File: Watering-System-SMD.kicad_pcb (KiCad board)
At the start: 2 copper layers, 76 x 30 mm, 20 parts, among them CON1 AVR-ISP-6, J1 Screw_Terminal_1x02, J2 CONN_01X04_MALE, J3 Screw_Terminal_1x04, J4 Screw_Terminal_1x02, Q1 MMBF170, Q2 2N7002, U1 MCP1703A-3302/MB, U2 ATTINY84-20SSU

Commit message: PCB routed
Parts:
- added M3: MountingHole_3.2mm_M3, Mounting_Holes:MountingHole_3.2mm_M3, F.Cu at (57.0, 95.0)
- added M3: MountingHole_3.2mm_M3, Mounting_Holes:MountingHole_3.2mm_M3, F.Cu at (125.0, 95.0)
- added U3: ESP-01, ESP8266:ESP-01, F.Cu at (98.8, 81.2)
- C3, D2, R1, R2: moved to B.Cu
- moved J2 24.1 mm to (68.7, 71.0), turned to 90 degrees
- moved C1 16.8 mm to (117.0, 90.5), turned to 90 degrees
- moved R5 15.5 mm to (107.5, 80.2), turned to 180 degrees
- moved R3 13.2 mm to (107.5, 82.5), turned to 180 degrees
- moved D1 11.8 mm to (121.2, 85.8), turned to 90 degrees
- moved Q2 11.6 mm to (56.8, 84.8), turned to 180 degrees
- moved U1 11.2 mm to (111.5, 90.5), turned to 0 degrees
- moved C2 10.2 mm to (106.5, 90.8), turned to 90 degrees
- moved C3 10.1 mm to (74.2, 89.5), turned to 90 degrees
- moved Q1 9.04 mm to (113.0, 81.2), turned to 90 degrees
- moved R4 7.77 mm to (61.9, 83.8)
- moved R6 7.65 mm to (61.9, 86.2)
- moved CON1 7.32 mm to (97.5, 88.2), turned to 270 degrees
- moved R1 4.74 mm to (56.2, 80.2)
- moved D2 4.07 mm to (112.5, 78.0)
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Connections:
- U2 pad 10: /RX -> /TX
- U2 pad 11: /TX -> /RX
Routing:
- net VCC: track 4.12 -> 136.3 mm, vias 0 -> 1
- net /SCL: track 0.00 -> 77.1 mm
- net /SDA: track 0.00 -> 72.4 mm
- net GND: track 0.00 -> 62.2 mm, vias 0 -> 2
- net /RX: track 0.00 -> 43.9 mm
- net /TX: track 0.00 -> 42.0 mm
- net /EV_ON: track 0.00 -> 33.6 mm, vias 0 -> 1
- net /SENSOR_ON: track 0.00 -> 19.9 mm
- net /RST: track 0.00 -> 19.4 mm, vias 0 -> 1
- net /EV_CONN: track 0.00 -> 13.6 mm
- net /SENSOR_CONN: track 0.00 -> 12.9 mm
- net Net-(Q1-Pad1): track 0.00 -> 4.11 mm
- net Net-(Q2-Pad1): track 0.00 -> 2.98 mm
- net Net-(C1-Pad1): track 15.0 -> 16.7 mm
- added copper zone on B.Cu, net GND
- added copper zone on F.Cu, net GND
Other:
- board text added: "9-12V/GND"
- board text added: "E.V."

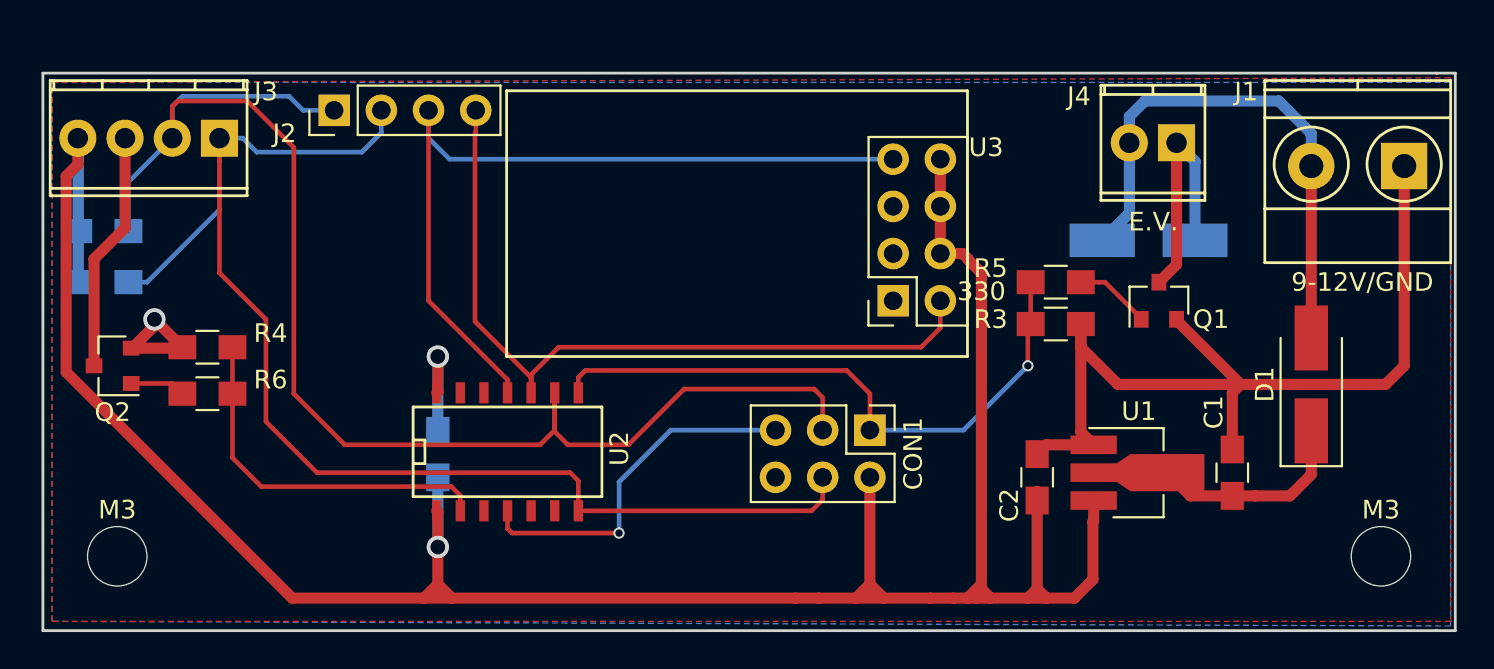
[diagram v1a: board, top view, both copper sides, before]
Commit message: SilkScreen changed
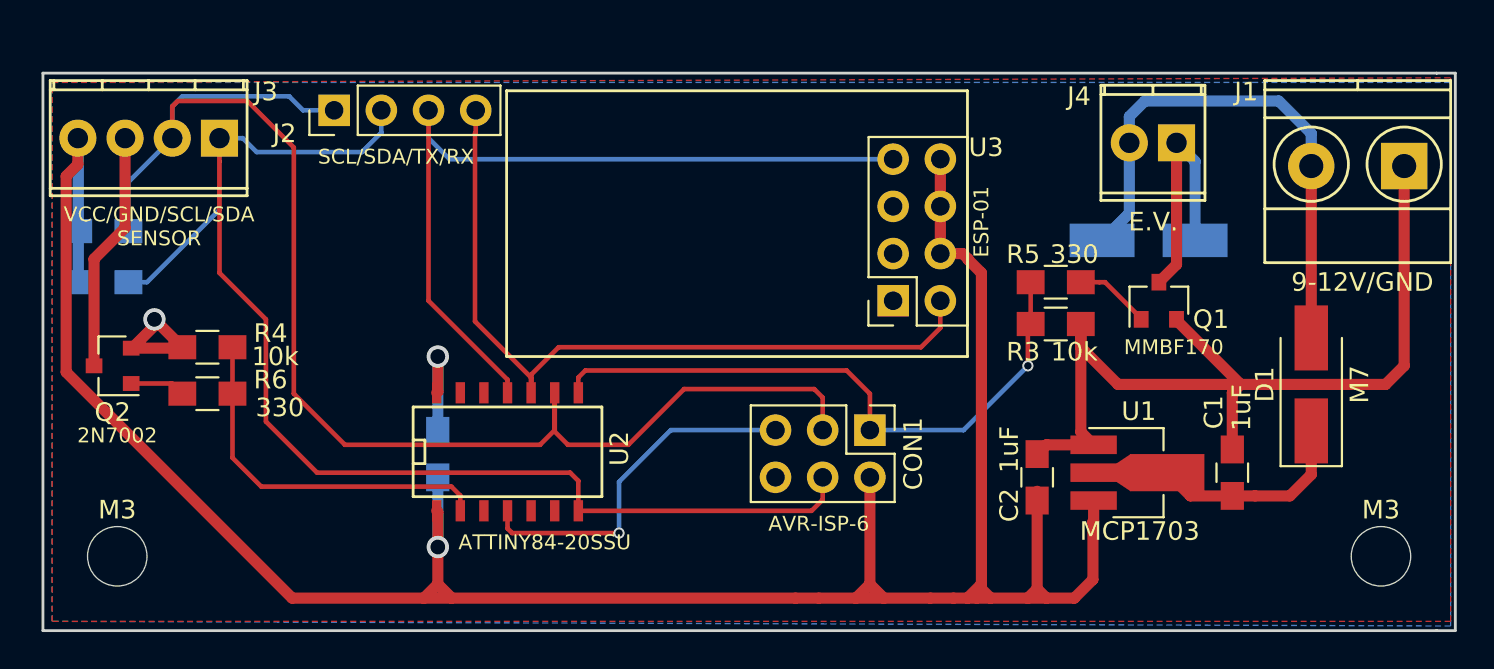
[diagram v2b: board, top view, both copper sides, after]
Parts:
- D1, D2: value D -> M7
- U1: value MCP1703A-3302/MB -> MCP1703
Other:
- board text added: "SCL/SDA/TX/RX"
- board text added: "VCC/GND/SCL/SDA SENSOR"
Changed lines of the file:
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@@
     (links 51)
     (no_connects 0)
-    (area 36.72143 63.678571 145.202382 108.7)
+    (area 52.924999 68.924999 129.075001 99.075001)
     (thickness 1.6)
-    (drawings 10)
+    (drawings 12)
     (tracks 189)
     (zones 0)
@@
   (page A4)
   (layers
-    (0 F.Cu signal)
-    (31 B.Cu signal)
+    (0 F.Cu signal hide)
+    (31 B.Cu signal hide)
     (32 B.Adhes user)
     (33 F.Adhes user)
@@
       (effects (font (size 1 1) (thickness 0.15)))
     )
-    (fp_text value ESP-01 (at 3.4925 5.08 90) (layer F.Fab)
-      (effects (font (size 1 1) (thickness 0.15)))
+    (fp_text value ESP-01 (at 4.25 4.75 90) (layer F.SilkS)
+      (effects (font (size 0.8 0.8) (thickness 0.15)))
     )
     (fp_line (start -3 -20.8) (end -3 4) (layer F.SilkS) (width 0.15))
@@
       (effects (font (size 1 1) (thickness 0.15)))
     )
-    (fp_text value 1uF (at 3.5 0.5 90) (layer F.Fab)
+    (fp_text value 1uF (at 3.5 0.5 90) (layer F.SilkS)
       (effects (font (size 1 1) (thickness 0.15)))
     )
@@
       (effects (font (size 1 1) (thickness 0.15)))
     )
-    (fp_text value 1uF (at 1.5 -1.5 90) (layer F.Fab)
+    (fp_text value 1uF (at 1.5 -1.5 90) (layer F.SilkS)
       (effects (font (size 1 1) (thickness 0.15)))
     )
@@
       (effects (font (size 1 1) (thickness 0.15)) (justify mirror))
     )
-    (fp_text value 0.1uF (at 0 -1.75 90) (layer B.Fab)
+    (fp_text value 0.1uF (at 0 -1.75 90) (layer B.SilkS)
       (effects (font (size 1 1) (thickness 0.15)) (justify mirror))
     )
@@
       (effects (font (size 1 1) (thickness 0.15)))
     )
-    (fp_text value AVR-ISP-6 (at 1.27 7.41 270) (layer F.Fab)
-      (effects (font (size 1 1) (thickness 0.15)))
+    (fp_text value AVR-ISP-6 (at 5.04 2.75 360) (layer F.SilkS)
+      (effects (font (size 0.8 0.8) (thickness 0.15)))
     )
     (fp_line (start -1.27 -1.27) (end -1.27 6.35) (layer F.Fab) (width 0.1))
@@
       (effects (font (size 1 1) (thickness 0.15)))
     )
-    (fp_text value MMBF170 (at -2.5 0.8 360) (layer F.Fab)
-      (effects (font (size 1 1) (thickness 0.15)))
+    (fp_text value MMBF170 (at -2.5 0.8 180) (layer F.SilkS)
+      (effects (font (size 0.8 0.8) (thickness 0.15)))
     )
     (fp_text user %R (at 0 0 90) (layer F.Fab)
@@
       (effects (font (size 1 1) (thickness 0.15)))
     )
-    (fp_text value 2N7002 (at 0 2.5 180) (layer F.Fab)
-      (effects (font (size 1 1) (thickness 0.15)))
+    (fp_text value 2N7002 (at -0.25 -3.75 180) (layer F.SilkS)
+      (effects (font (size 0.8 0.8) (thickness 0.15)))
     )
     (fp_text user %R (at -0.004762 0.535 180) (layer F.Fab)
@@
       (effects (font (size 1 1) (thickness 0.15)) (justify mirror))
     )
-    (fp_text value 4k7 (at -3.75 -0.75 180) (layer B.Fab)
+    (fp_text value 4k7 (at -3.75 -0.75 180) (layer B.SilkS)
       (effects (font (size 1 1) (thickness 0.15)) (justify mirror))
     )
@@
       (effects (font (size 1 1) (thickness 0.15)) (justify mirror))
     )
-    (fp_text value 4k7 (at -3.75 -0.75 180) (layer B.Fab)
+    (fp_text value 4k7 (at -3.75 -0.75 180) (layer B.SilkS)
       (effects (font (size 1 1) (thickness 0.15)) (justify mirror))
     )
@@
     (tags "resistor 0805")
     (attr smd)
-    (fp_text reference R3 (at 3.5 0.25 180) (layer F.SilkS)
-      (effects (font (size 1 1) (thickness 0.15)))
-    )
-    (fp_text value 10k (at 3.75 -1 180) (layer F.Fab)
+    (fp_text reference R3 (at 1.75 -1.5 180) (layer F.SilkS)
+      (effects (font (size 1 1) (thickness 0.15)))
+    )
+    (fp_text value 10k (at -1 -1.5 180) (layer F.SilkS)
       (effects (font (size 1 1) (thickness 0.15)))
     )
@@
       (effects (font (size 1 1) (thickness 0.15)))
     )
-    (fp_text value 10k (at 3.65 0.5) (layer F.Fab)
+    (fp_text value 10k (at 3.65 0.5) (layer F.SilkS)
       (effects (font (size 1 1) (thickness 0.15)))
     )
@@
     (tags "resistor 0805")
     (attr smd)
-    (fp_text reference R5 (at 3.5 0.75 180) (layer F.SilkS)
-      (effects (font (size 1 1) (thickness 0.15)))
-    )
-    (fp_text value 330 (at 4 -0.5 180) (layer F.SilkS)
+    (fp_text reference R5 (at 1.75 1.5 180) (layer F.SilkS)
+      (effects (font (size 1 1) (thickness 0.15)))
+    )
+    (fp_text value 330 (at -1 1.5 180) (layer F.SilkS)
       (effects (font (size 1 1) (thickness 0.15)))
     )
@@
       (effects (font (size 1 1) (thickness 0.15)))
     )
-    (fp_text value 330 (at 3.9 0.75) (layer F.Fab)
+    (fp_text value 330 (at 3.9 0.75) (layer F.SilkS)
       (effects (font (size 1 1) (thickness 0.15)))
     )
@@
       (effects (font (size 1 1) (thickness 0.15)))
     )
-    (fp_text value MCP1703A-3302/MB (at 0.5 3.15) (layer F.Fab)
+    (fp_text value MCP1703 (at 0.5 3.15) (layer F.SilkS)
       (effects (font (size 1 1) (thickness 0.15)))
     )
@@
       (effects (font (size 1 1) (thickness 0.15)))
     )
-    (fp_text value D (at 0 2.6 90) (layer F.Fab)
+    (fp_text value M7 (at 0 2.6 90) (layer F.SilkS)
       (effects (font (size 1 1) (thickness 0.15)))
     )
@@
       (effects (font (size 1 1) (thickness 0.15)) (justify mirror))
     )
-    (fp_text value D (at 0 -2.6) (layer B.Fab)
+    (fp_text value M7 (at 0 -2.6) (layer B.SilkS)
       (effects (font (size 1 1) (thickness 0.15)) (justify mirror))
     )
@@
       (effects (font (size 1 1) (thickness 0.15)))
     )
-    (fp_text value ATTINY84-20SSU (at 0 1.27) (layer F.Fab)
-      (effects (font (size 1 1) (thickness 0.15)))
+    (fp_text value ATTINY84-20SSU (at 2 5) (layer F.SilkS)
+      (effects (font (size 0.8 0.8) (thickness 0.15)))
     )
     (fp_line (start 5.08 -2.286) (end 5.08 2.54) (layer F.SilkS) (width 0.15))
@@
     (pad 1 np_thru_hole circle (at 0 0) (size 3.2 3.2) (drill 3.2) (layers *.Cu *.Mask))
   )
+  (gr_text "VCC/GND/SCL/SDA\nSENSOR" (at 59.25 77.25) (layer F.SilkS)
+    (effects (font (size 0.8 0.8) (thickness 0.2)))
+  )
+  (gr_text SCL/SDA/TX/RX (at 72 73.5) (layer F.SilkS)
+    (effects (font (size 0.8 0.8) (thickness 0.2)))
+  )
   (gr_text 9-12V/GND (at 124 80.25) (layer F.SilkS)

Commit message: gerber folder uploaded
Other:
- board text added: "Riego Automatico SMD V1.0 17-06-2017 J.Elío"
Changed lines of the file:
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@@
     (links 51)
     (no_connects 0)
-    (area 52.924999 68.924999 129.075001 99.075001)
+    (area 36.72143 63.678571 145.202382 108.7)
     (thickness 1.6)
-    (drawings 12)
+    (drawings 13)
     (tracks 189)
     (zones 0)
@@
     (visible_elements FFFFEF7F)
     (pcbplotparams
-      (layerselection 0x00030_80000001)
+      (layerselection 0x010f0_80000001)
       (usegerberextensions false)
       (excludeedgelayer true)
@@
       (outputformat 1)
       (mirror false)
-      (drillshape 1)
+      (drillshape 0)
       (scaleselection 1)
-      (outputdirectory ""))
+      (outputdirectory Gerbers))
   )
   (net 0 "")
@@
     (pad 1 np_thru_hole circle (at 0 0) (size 3.2 3.2) (drill 3.2) (layers *.Cu *.Mask))
   )
+  (gr_text "Riego Automatico SMD\nV1.0 17-06-2017 J.Elío\n" (at 60.75 97) (layer F.SilkS)
+    (effects (font (size 0.8 0.8) (thickness 0.15) italic) (justify left))
+  )
   (gr_text "VCC/GND/SCL/SDA\nSENSOR" (at 59.25 77.25) (layer F.SilkS)
